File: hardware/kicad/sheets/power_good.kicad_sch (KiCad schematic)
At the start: 5 parts, among them Q10 BSS138

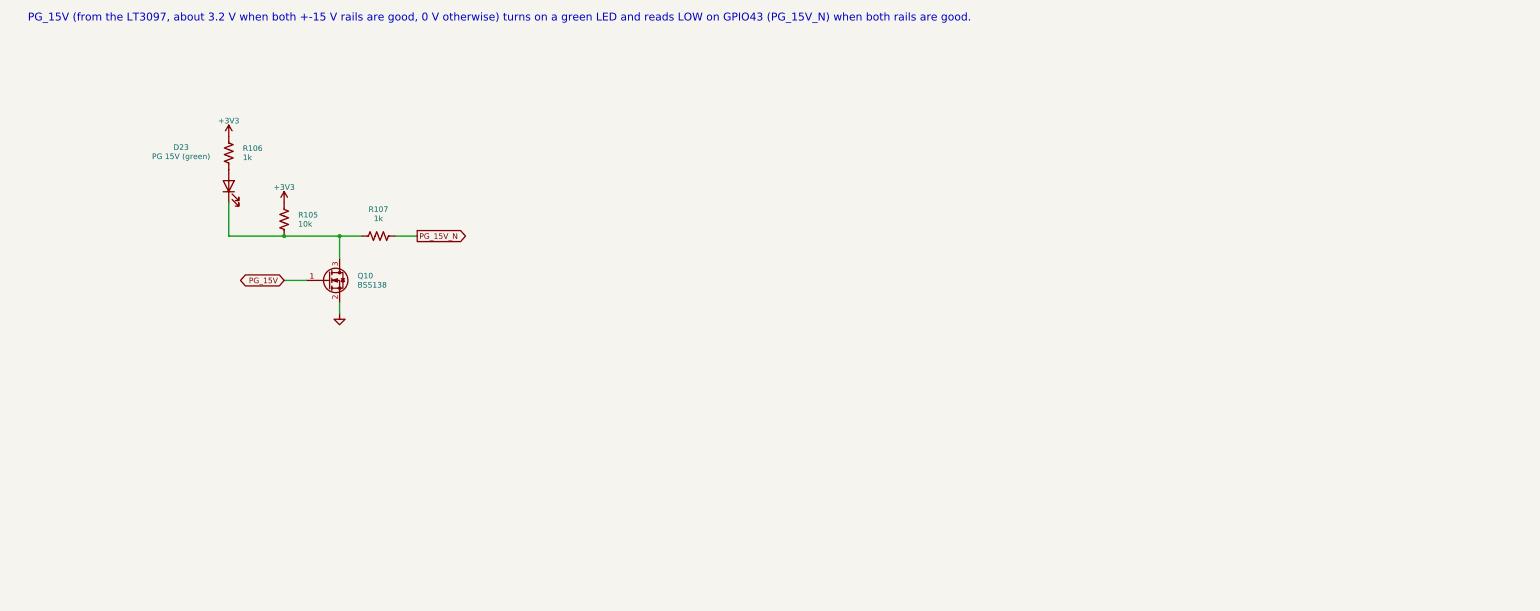
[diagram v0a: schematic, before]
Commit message: Log +-15 V power-good changes and add one LED per LT3097 PG pin
Firmware
- amplifier: configure PG_15V_N_PIN (GPIO43, active LOW), log the starting
  state and every debounced change (PowerGoodMonitor in power_good.h);
  amplifier::isPowerGood() reports the level. The lines reach the dashboard
  console through the logger ring buffer.
- dashboard: console colours for "power lost" (red), "power restored" and
  "power good: yes" (green), "power good: no" (yellow).
- native tests for the debounce logic and the amplifier stub.

Hardware
- power_good sheet: PGP and PGN each drive their own node (220k/62k from
  +15 V) and a green LED (D24 +15 V, D25 -15 V) through a BSS138W; a BAT54AW
  with a 10k pull-up ANDs the nodes into PG_15V, so the REM interlock and the
  PG_15V_N flag are unchanged.
- 0402 resistors, SOT-323 FETs and one BAT54AW so the stage fits the power
  box; Power Good parts are placed last in gen_pcb.py.
- Board re-routed with Freerouting 2.5.0 and cleaned with fix_route.py: DRC
  0 unconnected, no copper violations. Gerbers, JLCPCB zip, renders, BOM, CPL
  and schematic PDF regenerated; datasheet rules 193/193.

Co-Authored-By: Claude Sonnet 5.5 <noreply@anthropic.com>
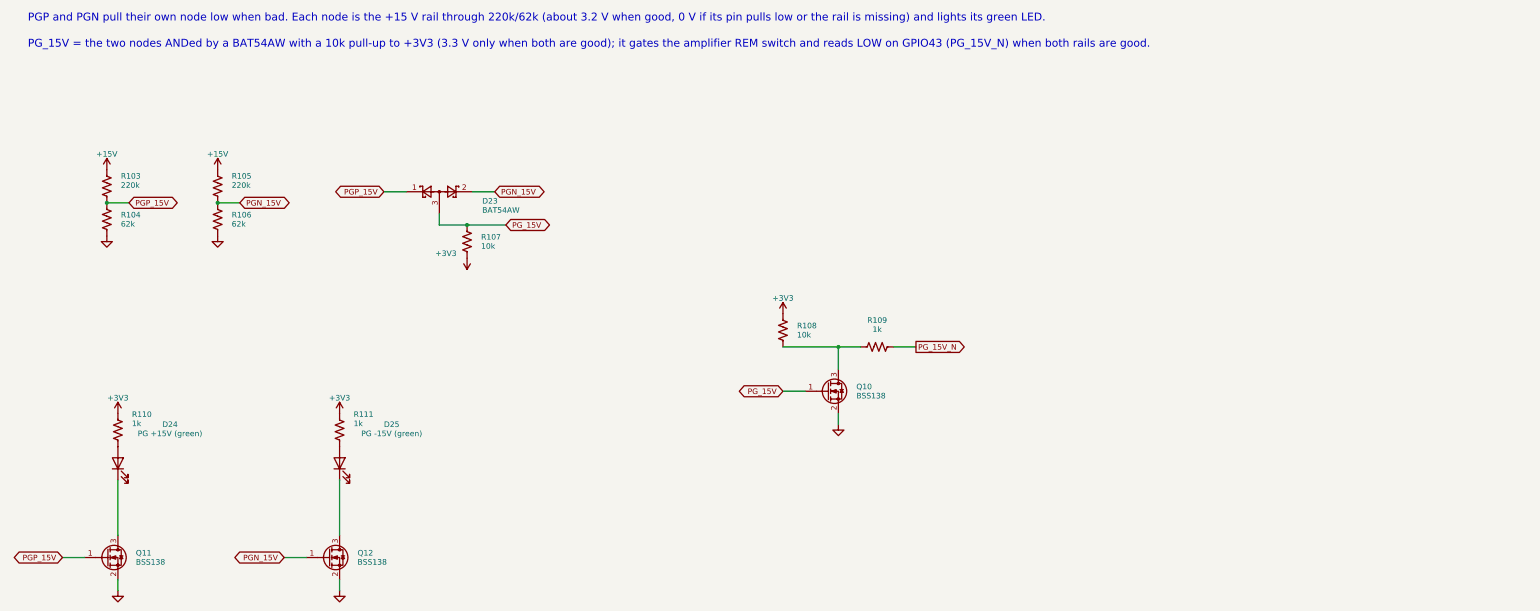
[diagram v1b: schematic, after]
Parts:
- removed R107: 1k, Resistor_SMD:R_0603_1608Metric, symbol Device:R_US
- added D23: BAT54AW, Package_TO_SOT_SMD:SOT-323_SC-70, symbol Diode:BAT54AW
- added D24: PG +15V (green), LED_SMD:LED_0402_1005Metric, symbol Device:LED
- added D25: PG -15V (green), LED_SMD:LED_0402_1005Metric, symbol Device:LED
- added Q11, Q12: BSS138, Package_TO_SOT_SMD:SOT-323_SC-70, symbol Transistor_FET:BSS138
- added R103: 220k, Resistor_SMD:R_0402_1005Metric, symbol Device:R_US
- added R104: 62k, Resistor_SMD:R_0402_1005Metric, symbol Device:R_US
- added R108: 10k, Resistor_SMD:R_0402_1005Metric, symbol Device:R_US
- added R109, R110, R111: 1k, Resistor_SMD:R_0402_1005Metric, symbol Device:R_US
- Q10: footprint Package_TO_SOT_SMD:SOT-23 -> Package_TO_SOT_SMD:SOT-323_SC-70
- R105: value 10k -> 220k; footprint Resistor_SMD:R_0603_1608Metric -> Resistor_SMD:R_0402_1005Metric
- R106: value 1k -> 62k; footprint Resistor_SMD:R_0603_1608Metric -> Resistor_SMD:R_0402_1005Metric
- R107: renamed from D23; value PG 15V (green) -> 10k; footprint LED_SMD:LED_0603_1608Metric -> Resistor_SMD:R_0402_1005Metric; symbol Device:LED -> Device:R_US
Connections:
- net +3V3: now also R107.2, R108.1, R110.1, R111.1; no longer R105.1, R106.1
- net GND: now also R106.2, Q11.2 (S), Q12.2 (S), R104.2
- net PG_15V: now also R107.1, D23.3
- net PG_15V_N: now also R109.2
- new net: D25.1 (K), Q12.3 (D)
- new net: D25.2 (A), R111.2
- new net: D24.1 (K), Q11.3 (D)
- new net: D24.2 (A), R110.2
- new net: Q10.3 (D), R108.2, R109.1
- new net +15V: R103.1, R105.1
- new net PGN_15V: D23.2, Q12.1 (G), R105.2, R106.1
- new net PGP_15V: D23.1, Q11.1 (G), R103.2, R104.1
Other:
- note added: "PGP and PGN pull their own node low when bad. Each node is the +15 V rail through 220k/62k (about 3.2 V when good, 0 V if its pin pulls low or the rail is missing) and lights its green LED."
- note added: "PG_15V = the two nodes ANDed by a BAT54AW with a 10k pull-up to +3V3 (3.3 V only when both are good); it gates the amplifier REM switch and reads LOW on GPIO43 (PG_15V_N) when both rails are good."
- note removed: "PG_15V (from the LT3097, about 3.2 V when both +-15 V rails are good, 0 V otherwise) turns on a green LED and reads LOW on GPIO43 (PG_15V_N) when both rails are good."
- moved on the sheet: R105, R107

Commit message: WIP: restructure PCB for the Phoenix UCS 125-87 housing
Work in progress, layout not finished: about 90 parts still do not fit
their sections and the board is not routed.

- Right-angle connectors: Phoenix MSTBA 2,5 / MC 1,5, JST XH side entry,
  Hirose DF13, Molex 505448-0871 (new footprint from the Molex drawing)
- Datasheet and product links on every symbol (tools/part_links.py)
- Test points so every IC has one on its own nets
- gen_pcb.py: 100 x 62 mm two-sided board, housing holes and restricted
  corners, ESP32 antenna notch, one section per sheet, board ID block,
  ESP32 pin names, pin-1 marks, blue mask
- Housing drawings in hardware/housing/

Co-Authored-By: Claude Opus 5.5 <noreply@anthropic.com>
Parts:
- removed D24: PG +15V (green), LED_SMD:LED_0402_1005Metric, symbol Device:LED
- removed R104, R106: 62k, Resistor_SMD:R_0402_1005Metric, symbol Device:R_US
- removed R108: 10k, Resistor_SMD:R_0402_1005Metric, symbol Device:R_US
- removed R109: 1k, Resistor_SMD:R_0402_1005Metric, symbol Device:R_US
- added Q10, Q11, Q12: BSS138, Package_TO_SOT_SMD:SOT-323_SC-70, symbol Transistor_FET:BSS138
- added R107: 10k, Resistor_SMD:R_0402_1005Metric, symbol Device:R_US
- added R111: 1k, Resistor_SMD:R_0402_1005Metric, symbol Device:R_US
- D23: renamed from Q10; value BSS138 -> BAT54AW; symbol Transistor_FET:BSS138 -> Diode:BAT54AW; Product (none) -> https://www.digikey.com/en/products/result?keywords=BAT54AW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
- D24: renamed from R111; value 1k -> PG +15V (green); footprint Resistor_SMD:R_0402_1005Metric -> LED_SMD:LED_0402_1005Metric; symbol Device:R_US -> Device:LED; Product (none) -> https://www.digikey.com/en/products/result?keywords=APG1005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
- D25: Product (none) -> https://www.digikey.com/en/products/result?keywords=APG1005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
- R103: Product (none) -> https://www.digikey.com/en/products/result?keywords=RC0402F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
- R104: renamed from R105; value 220k -> 62k; Product (none) -> https://www.digikey.com/en/products/result?keywords=RC0402F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
- R105: renamed from D23; value BAT54AW -> 220k; footprint Package_TO_SOT_SMD:SOT-323_SC-70 -> Resistor_SMD:R_0402_1005Metric; symbol Diode:BAT54AW -> Device:R_US; Product (none) -> https://www.digikey.com/en/products/result?keywords=RC0402F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
- R106: renamed from R107; value 10k -> 62k; Product (none) -> https://www.digikey.com/en/products/result?keywords=RC0402F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
- R108: renamed from Q11; value BSS138 -> 10k; footprint Package_TO_SOT_SMD:SOT-323_SC-70 -> Resistor_SMD:R_0402_1005Metric; symbol Transistor_FET:BSS138 -> Device:R_US; Product (none) -> https://www.digikey.com/en/products/result?keywords=RC0402F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
- R109: renamed from R110; Product (none) -> https://www.digikey.com/en/products/result?keywords=RC0402F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
- R110: renamed from Q12; value BSS138 -> 1k; footprint Package_TO_SOT_SMD:SOT-323_SC-70 -> Resistor_SMD:R_0402_1005Metric; symbol Transistor_FET:BSS138 -> Device:R_US; Product (none) -> https://www.digikey.com/en/products/result?keywords=RC0402F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
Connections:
- net +15V: now also R105.1; no longer R104.1
- net +3V3: now also R108.1, R110.1, R107.2, R111.1; no longer D24.1, R106.2, R109.1
- net GND: now also R104.2, R106.2, Q10.2 (S), Q11.2 (S), Q12.2 (S); no longer D23.2 (S), R108.2 (S), R110.2 (S)
- net PGN_15V: now also D23.2, R106.1, Q12.1 (G); no longer R104.2, R110.1 (G)
- net PGP_15V: now also D23.1, R104.1, Q11.1 (G); no longer R105.1, R108.1 (G)
- net PG_15V: now also D23.3, Q10.1 (G), R107.1; no longer D23.1 (G), R105.3, R106.1
- net PG_15V_N: now also R109.2
- net at D25.1 (K): now also Q12.3 (D); no longer R110.3 (D)
- net at D24.2 (A): now also R110.2; no longer D25.2 (A)
- new net: D25.2 (A), R111.2
- new net: D24.1 (K), Q11.3 (D)
- new net: Q10.3 (D), R108.2, R109.1
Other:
- moved on the sheet: D23, D24, R104, R106, R109

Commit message: Ground the M12 shield, order the ground loops, name the J14 cable parts
- J10: shielded symbol (Conn_01x04_Shielded); the M12 shield pin and its
  four shell legs are pad SH, tied to GND
- TP22-TP25: Keystone 5001 black miniature PC test points (KiCad
  TestPoint_Keystone_5000-5004 footprint, 1.02 mm hole per Keystone's
  drawing); now in the BOM, the bare pad test points stay out
- J14 BOM note: cable housing Molex 5054320801 with 505431 terminals, or
  tin pre-crimped leads 797581148 / 797581149 (from molex.com)

Only netlist change: GND gains J10 SH. DRC 0 errors, 0 unconnected, 0
schematic-parity issues; ERC 0; 193/193 datasheet rules.

Co-Authored-By: Claude Opus 5.5 <noreply@anthropic.com>
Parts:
- removed D23: BAT54AW, Package_TO_SOT_SMD:SOT-323_SC-70, symbol Diode:BAT54AW
- removed D24: PG +15V (green), LED_SMD:LED_0402_1005Metric, symbol Device:LED
- removed R103, R105: 220k, Resistor_SMD:R_0402_1005Metric, symbol Device:R_US
- removed R109: 1k, Resistor_SMD:R_0402_1005Metric, symbol Device:R_US
- added Q11, Q12: BSS138, Package_TO_SOT_SMD:SOT-323_SC-70, symbol Transistor_FET:BSS138
- added R104, R106: 62k, Resistor_SMD:R_0402_1005Metric, symbol Device:R_US
- added R107: 10k, Resistor_SMD:R_0402_1005Metric, symbol Device:R_US
- D23: renamed from R107; value 10k -> BAT54AW; footprint Resistor_SMD:R_0402_1005Metric -> Package_TO_SOT_SMD:SOT-323_SC-70; symbol Device:R_US -> Diode:BAT54AW; Product https://www.digikey.com/en/products/result?keywords=RC0402F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 -> https://www.digikey.com/en/products/result?keywords=BAT54AW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
- D24: renamed from Q12; value BSS138 -> PG +15V (green); footprint Package_TO_SOT_SMD:SOT-323_SC-70 -> LED_SMD:LED_0402_1005Metric; symbol Transistor_FET:BSS138 -> Device:LED; Product https://www.digikey.com/en/products/result?keywords=BSS138W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 -> https://www.digikey.com/en/products/result?keywords=APG1005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
- R103: renamed from R104; value 62k -> 220k; Product https://www.digikey.com/en/products/result?keywords=RC0402FR-0762KL -> https://www.digikey.com/en/products/result?keywords=RC0402FR-07220KL
- R105: renamed from R106; value 62k -> 220k; Product https://www.digikey.com/en/products/result?keywords=RC0402FR-0762KL -> https://www.digikey.com/en/products/result?keywords=RC0402FR-07220KL
- R109: renamed from Q11; value BSS138 -> 1k; footprint Package_TO_SOT_SMD:SOT-323_SC-70 -> Resistor_SMD:R_0402_1005Metric; symbol Transistor_FET:BSS138 -> Device:R_US; Product https://www.digikey.com/en/products/result?keywords=BSS138W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 -> https://www.digikey.com/en/products/result?keywords=RC0402F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
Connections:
- net +15V: now also R103.1, R105.1
- net +3V3: now also R107.2; no longer D23.2
- net GND: now also Q11.2 (S), Q12.2 (S), R104.2, R106.2; no longer D24.2 (S), R103.2, R105.2, R109.2 (S)
- net PGN_15V: now also D23.2, R105.2, Q12.1 (G), R106.1; no longer D24.1 (G), R105.1
- net PGP_15V: now also D23.1, R103.2, Q11.1 (G), R104.1; no longer R103.1, R109.1 (G)
- net PG_15V: now also D23.3, R107.1; no longer D23.1
- net PG_15V_N: now also R109.2
- net at R110.2: now also D24.2 (A)
- net at D25.1 (K): now also Q12.3 (D); no longer D24.3 (D)
- net at Q10.3 (D), R108.2: now also R109.1
- new net: D24.1 (K), Q11.3 (D)
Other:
- moved on the sheet: R103, R105
